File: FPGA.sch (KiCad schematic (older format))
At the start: 0 parts

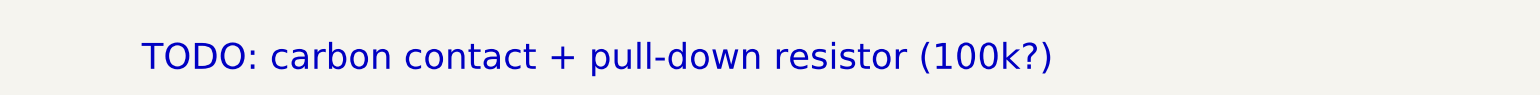
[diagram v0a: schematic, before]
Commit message: Add placeholder sheets for functions to be implemented
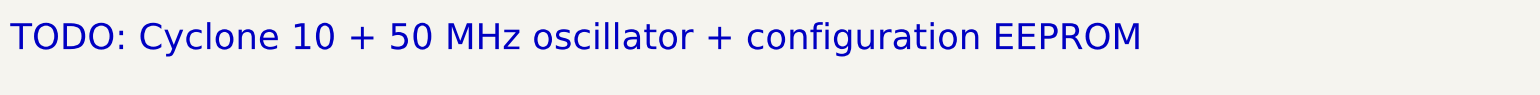
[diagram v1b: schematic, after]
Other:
- note added: "TODO: Cyclone 10 + 50 MHz oscillator + configuration EEPROM"
- note removed: "TODO: carbon contact + pull-down resistor (100k?)"
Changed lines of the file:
@@
 $Descr A4 11693 8268
 encoding utf-8
-Sheet 10 16
-Title "Litter Robot 3 - Push button"
-Date "2021-02-28"
+Sheet 15 16
+Title "Litter Robot 3 - FPGA"
+Date "2021-03-02"
 Rev "A1"
 Comp "L. Sartory"
@@
 Comment4 ""
 $EndDescr
-Text Notes 2000 4100 0    197  ~ 0
-TODO: carbon contact + pull-down resistor (100k?)
+Text Notes 1000 3950 0    197  ~ 0
+TODO: Cyclone 10 + 50 MHz oscillator + configuration EEPROM
 $EndSCHEMATC

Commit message: Add TODO notes
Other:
- note added: "TODO:\n- Cyclone 10 (10CL016YE144C8G)\n- Oscillator (KC7050K16.3840C1GE00)\n- Configuration EEPROM (MT25QL128ABA8ESF-0AAT)"
- note removed: "TODO: Cyclone 10 + 50 MHz oscillator + configuration EEPROM"
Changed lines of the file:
@@
 Comment4 ""
 $EndDescr
-Text Notes 1000 3950 0    197  ~ 0
-TODO: Cyclone 10 + 50 MHz oscillator + configuration EEPROM
+Text Notes 1500 4150 0    197  ~ 0
+TODO:\n- Cyclone 10 (10CL016YE144C8G)\n- Oscillator (KC7050K16.3840C1GE00)\n- Configuration EEPROM (MT25QL128ABA8ESF-0AAT)
 $EndSCHEMATC

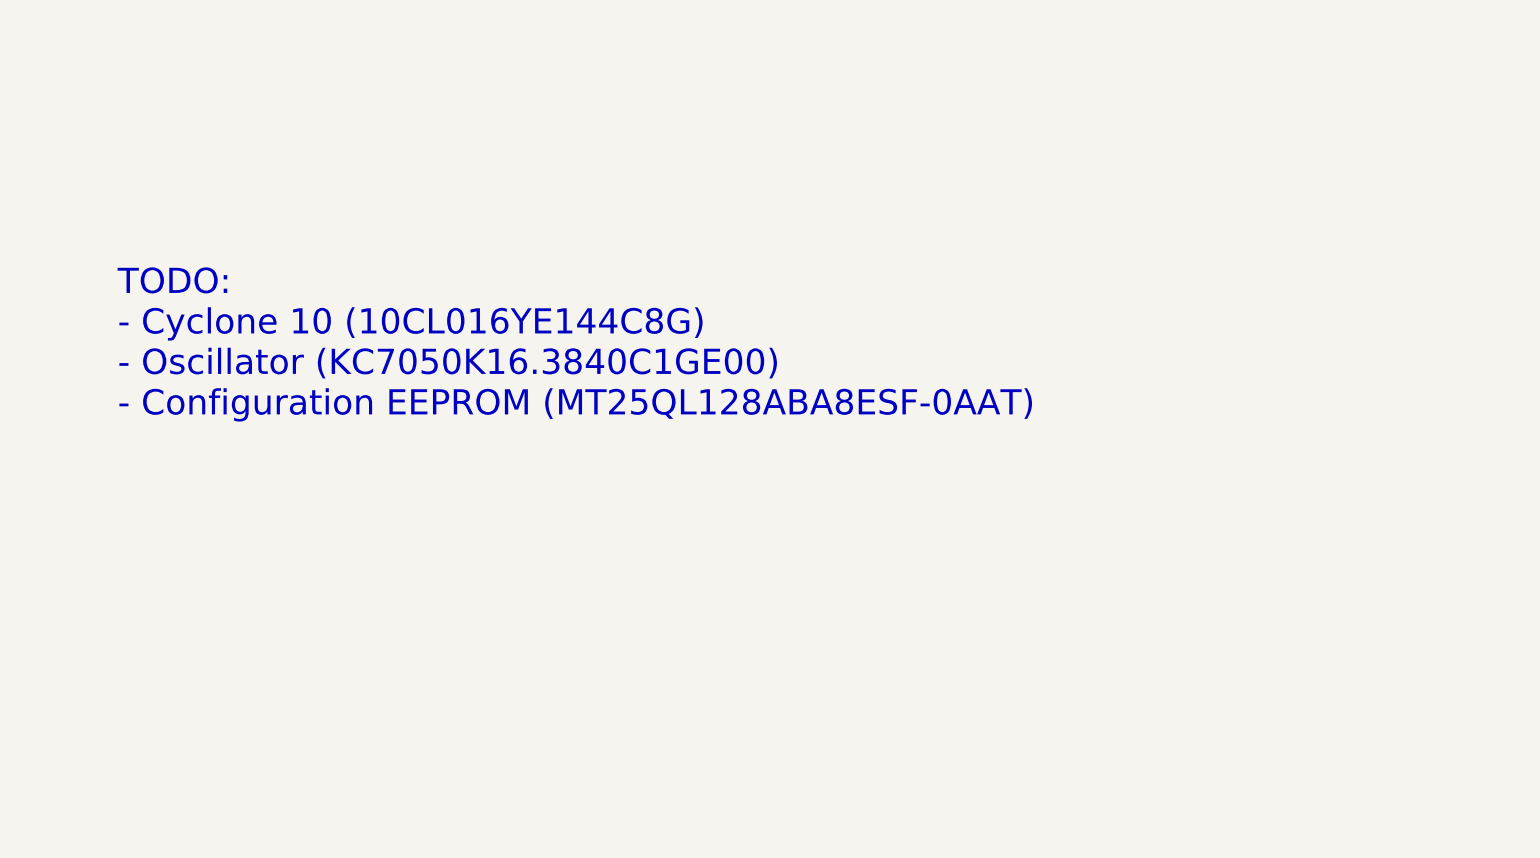
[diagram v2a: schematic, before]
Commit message: Add fuse and more inter-page signals
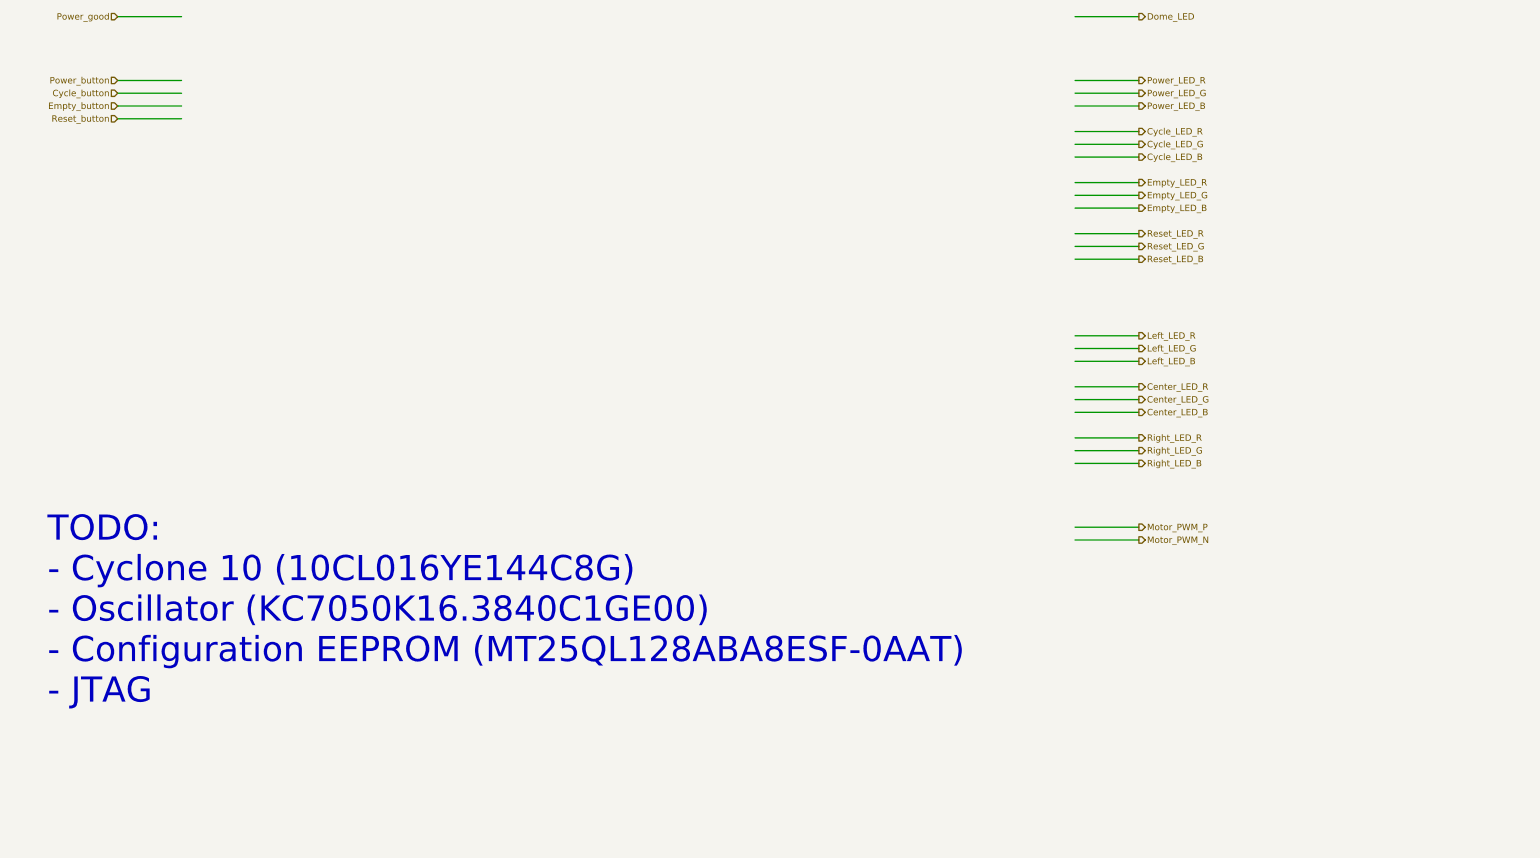
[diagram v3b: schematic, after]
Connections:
- net labels added: Center_LED_B, Center_LED_G, Center_LED_R, Cycle_LED_B, Cycle_LED_G, Cycle_LED_R, Cycle_button, Dome_LED, Empty_LED_B, Empty_LED_G, Empty_LED_R, Empty_button, Left_LED_B, Left_LED_G, Left_LED_R, Motor_PWM_N, Motor_PWM_P, Power_LED_B, Power_LED_G, Power_LED_R, Power_button, Power_good, Reset_LED_B, Reset_LED_G, Reset_LED_R, Reset_button, Right_LED_B, Right_LED_G, Right_LED_R
- wire segments 0 -> 29
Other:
- note added: "TODO:\n- Cyclone 10 (10CL016YE144C8G)\n- Oscillator (KC7050K16.3840C1GE00)\n- Configuration EEPROM (MT25QL128ABA8ESF-0AAT)\n- JTAG"
- note removed: "TODO:\n- Cyclone 10 (10CL016YE144C8G)\n- Oscillator (KC7050K16.3840C1GE00)\n- Configuration EEPROM (MT25QL128ABA8ESF-0AAT)"
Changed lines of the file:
@@
 Comment4 ""
 $EndDescr
-Text Notes 1500 4150 0    197  ~ 0
-TODO:\n- Cyclone 10 (10CL016YE144C8G)\n- Oscillator (KC7050K16.3840C1GE00)\n- Configuration EEPROM (MT25QL128ABA8ESF-0AAT)
+Text HLabel 1500 1600 0    50   Input ~ 0
+Cycle_button
+Text HLabel 1500 1700 0    50   Input ~ 0
+Empty_button
+Text HLabel 1500 1800 0    50   Input ~ 0
+Reset_button
+Text HLabel 9500 1900 2    50   Output ~ 0
+Cycle_LED_R
+Text HLabel 9500 2000 2    50   Output ~ 0
+Cycle_LED_G
+Text HLabel 9500 2100 2    50   Output ~ 0
+Cycle_LED_B
+Wire Wire Line
+	9500 1900 9000 1900
+Wire Wire Line
+	9500 2000 9000 2000
+Wire Wire Line
+	9500 2100 9000 2100
+Text HLabel 9500 2300 2    50   Output ~ 0
+Empty_LED_R
+Text HLabel 9500 2400 2    50   Output ~ 0
+Empty_LED_G
+Text HLabel 9500 2500 2    50   Output ~ 0
+Empty_LED_B
+Wire Wire Line
+	9500 2300 9000 2300
+Wire Wire Line
+	9500 2400 9000 2400
+Wire Wire Line
+	9500 2500 9000 2500
+Text HLabel 9500 2700 2    50   Output ~ 0
+Reset_LED_R
+Text HLabel 9500 2800 2    50   Output ~ 0
+Reset_LED_G
+Text HLabel 9500 2900 2    50   Output ~ 0
+Reset_LED_B
+Wire Wire Line
+	9500 2700 9000 2700
+Wire Wire Line
+	9500 2800 9000 2800
+Wire Wire Line
+	9500 2900 9000 2900
+Text HLabel 9500 3500 2    50   Output ~ 0
+Left_LED_R
+Text HLabel 9500 3600 2    50   Output ~ 0
+Left_LED_G
+Text HLabel 9500 3700 2    50   Output ~ 0
+Left_LED_B
+Wire Wire Line
+	9500 3500 9000 3500
+Wire Wire Line
+	9500 3600 9000 3600
+Wire Wire Line
+	9500 3700 9000 3700
+Text HLabel 9500 3900 2    50   Output ~ 0
+Center_LED_R
+Text HLabel 9500 4000 2    50   Output ~ 0
+Center_LED_G
+Text HLabel 9500 4100 2    50   Output ~ 0
+Center_LED_B
+Wire Wire Line
+	9500 3900 9000 3900
+Wire Wire Line
+	9500 4000 9000 4000
+Wire Wire Line
+	9500 4100 9000 4100
+Text HLabel 9500 4300 2    50   Output ~ 0
+Right_LED_R
+Text HLabel 9500 4400 2    50   Output ~ 0
+Right_LED_G
+Text HLabel 9500 4500 2    50   Output ~ 0
+Right_LED_B
+Wire Wire Line
+	9500 4300 9000 4300
+Wire Wire Line
+	9500 4400 9000 4400
+Wire Wire Line
+	9500 4500 9000 4500
+Text HLabel 1500 1500 0    50   Input ~ 0
+Power_button
+Wire Wire Line
+	1500 1500 2000 1500
+Wire Wire Line
+	1500 1600 2000 1600
+Wire Wire Line
+	1500 1700 2000 1700
+Wire Wire Line
+	1500 1800 2000 1800
+Text HLabel 1500 1000 0    50   Input ~ 0
+Power_good
+Wire Wire Line
+	1500 1000 2000 1000
+Wire Wire Line
+	9500 1700 9000 1700
+Wire Wire Line
+	9500 1600 9000 1600
+Wire Wire Line
+	9500 1500 9000 1500
+Text HLabel 9500 1700 2    50   Output ~ 0
+Power_LED_B
+Text HLabel 9500 1600 2    50   Output ~ 0
+Power_LED_G
+Text HLabel 9500 1500 2    50   Output ~ 0
+Power_LED_R
+Wire Wire Line
+	9000 5100 9500 5100
+Wire Wire Line
+	9000 5000 9500 5000
+Text HLabel 9500 5100 2    50   Output ~ 0
+Motor_PWM_N
+Text HLabel 9500 5000 2    50   Output ~ 0
+Motor_PWM_P
+Text Notes 950  6400 0    197  ~ 0
+TODO:\n- Cyclone 10 (10CL016YE144C8G)\n- Oscillator (KC7050K16.3840C1GE00)\n- Configuration EEPROM (MT25QL128ABA8ESF-0AAT)\n- JTAG
+Wire Wire Line
+	9000 1000 9500 1000
+Text HLabel 9500 1000 2    50   Output ~ 0
+Dome_LED
 $EndSCHEMATC

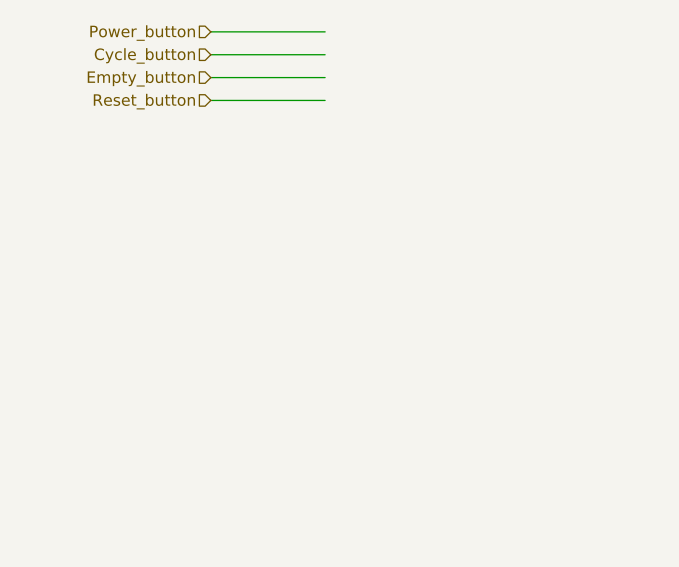
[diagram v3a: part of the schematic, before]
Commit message: Add an ambient light sensor
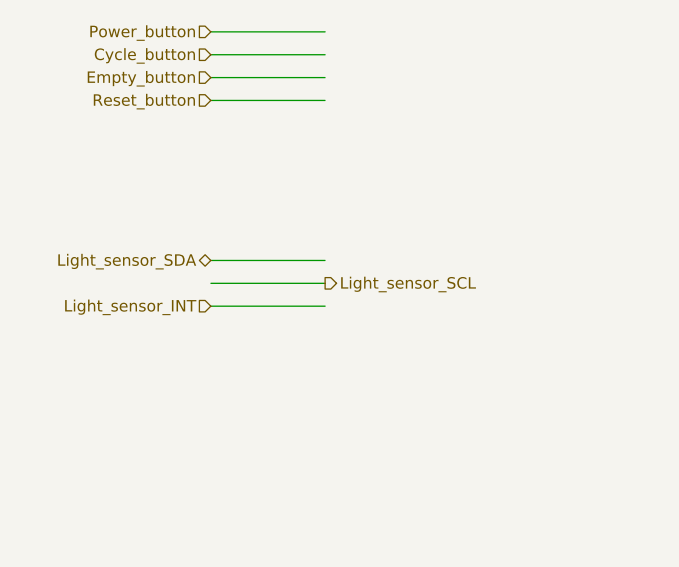
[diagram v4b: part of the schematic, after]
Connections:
- net labels added: Light_sensor_INT, Light_sensor_SCL, Light_sensor_SDA
- wire segments 29 -> 32
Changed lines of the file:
@@
 $Descr A4 11693 8268
 encoding utf-8
-Sheet 15 16
+Sheet 15 17
 Title "Litter Robot 3 - FPGA"
 Date "2021-03-02"
@@
 Text HLabel 9500 1000 2    50   Output ~ 0
 Dome_LED
+Wire Wire Line
+	1500 2700 2000 2700
+Text HLabel 1500 2500 0    50   BiDi ~ 0
+Light_sensor_SDA
+Text HLabel 2000 2600 2    50   Output ~ 0
+Light_sensor_SCL
+Text HLabel 1500 2700 0    50   Input ~ 0
+Light_sensor_INT
+Wire Wire Line
+	2000 2500 1500 2500
+Wire Wire Line
+	1500 2600 2000 2600
 $EndSCHEMATC
